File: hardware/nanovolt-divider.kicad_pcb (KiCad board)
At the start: 2 copper layers, 100 x 62 mm, 76 parts, among them J1 NORMAL IN +, J2 NORMAL IN -, J3 HV IN +, J4 HV IN -, J5 DIVIDER OUT HI, J6 DIVIDER OUT LO, J7 ESP32_DISP_P1, J8 ESP32_DISP_CN1, J9 ESP32_DISP_P3, K1 TQ2-L2-5V, K2 TQ2-L2-5V, K3 TQ2-L2-5V, K4 TQ2-L2-5V, K5 TQ2-L2-5V, Q1 MMBT2222A, Q10 MMBT2222A, Q2 MMBT2222A, Q3 MMBT2222A, Q4 MMBT2222A, Q5 MMBT2222A, Q6 MMBT2222A, Q7 MMBT2222A, Q8 MMBT2222A, Q9 MMBT2222A, SW1 SW_3PDT NORMAL/HV, U1 MCP23017-E/SO, U2 TMP117MAIYBGR

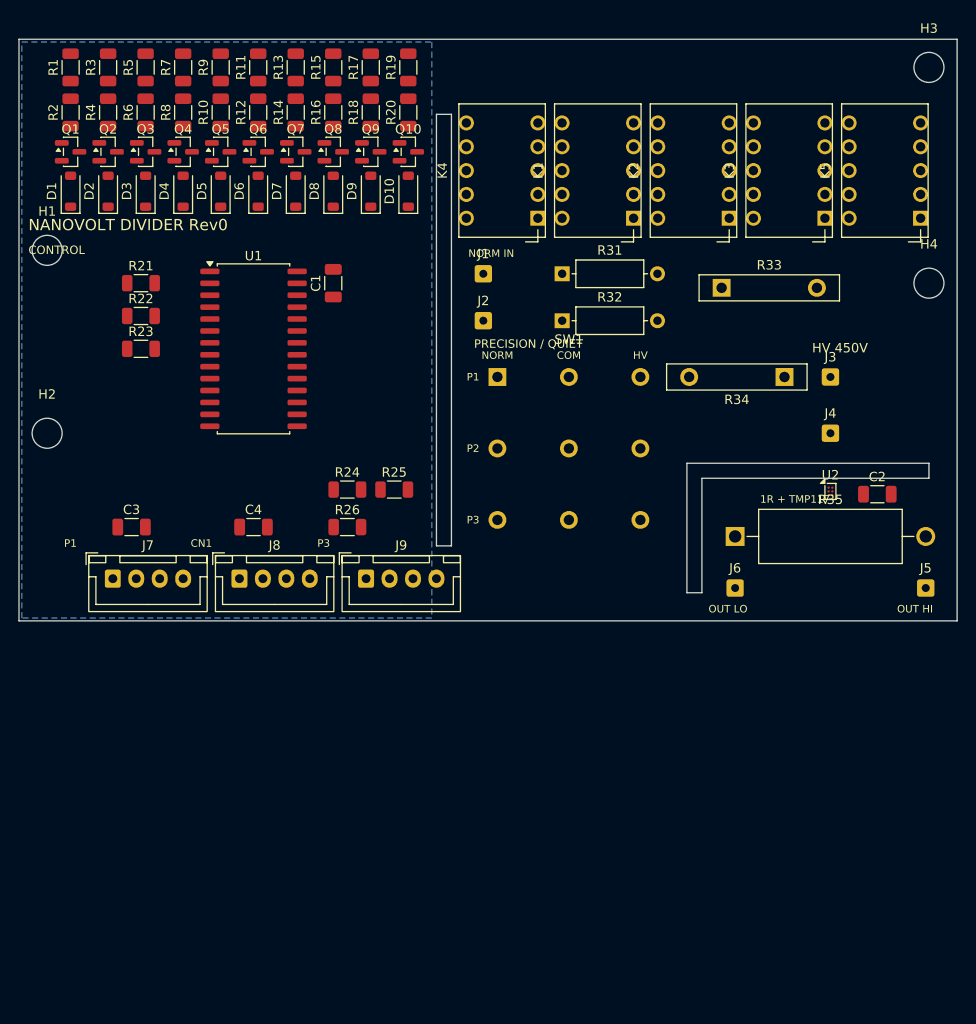
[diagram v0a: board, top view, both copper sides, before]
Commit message: PCB: portrait top-down layout, notch-isolated 1 ohm strip
- 60 x 103 mm: harness connectors, MCP23017 (horizontal, flanked by
  caps and pull-ups), coil drivers above their relays, relay row, then
  the quiet section (high legs, 3PDT pads, HV, 1 ohm strip)
- 1 ohm strip isolated by two edge notches with a 10 mm centre bridge
  for MEAS / return / TMP117 lines; driver-to-relay slot removed
- DRC: only unrouted ratsnest and silkscreen warnings remain

Co-Authored-By: Claude Fable 5.1 <noreply@anthropic.com>
Claude-Session: https://claude.ai/code/session_012iVAGTG9sDDBFakz9fB6fg
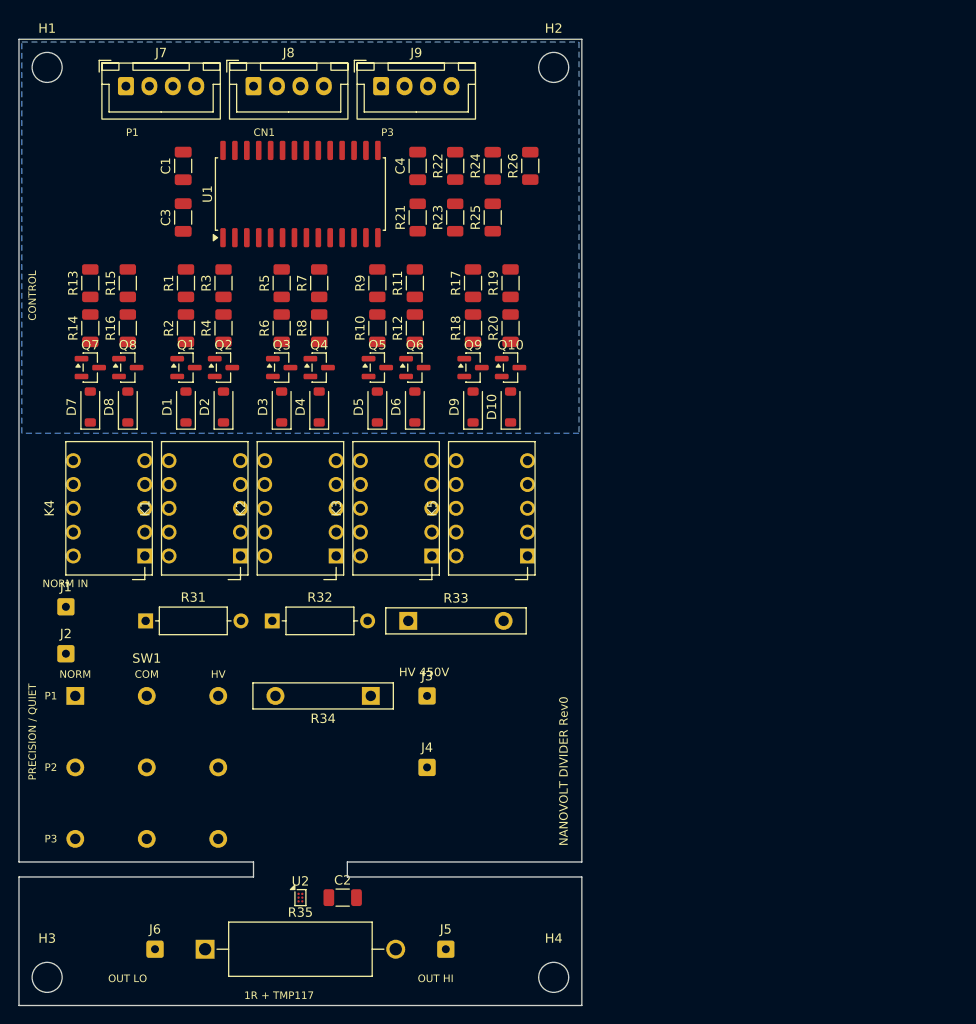
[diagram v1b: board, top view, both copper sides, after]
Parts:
- moved H3 135.1 mm to (53.0, 150.0)
- moved H4 84.1 mm to (107.0, 150.0)
- moved J6 72.8 mm to (64.5, 147.0)
- moved R35 71.6 mm to (69.8, 147.0)
- moved C2 71.4 mm to (84.5, 141.5)
- moved U2 71.2 mm to (80.0, 141.5)
- moved H2 66.6 mm to (107.0, 53.0)
- moved J5 64.0 mm to (95.5, 147.0)
- moved R31 57.8 mm to (63.5, 112.0)
- moved J1 56.9 mm to (55.0, 110.5)
- moved J2 56.9 mm to (55.0, 115.5)
- moved SW1 56.4 mm to (56.0, 120.0)
- moved J4 55.8 mm to (93.5, 127.6)
- moved R34 55.7 mm to (87.5, 120.0)
- moved K1 55.2 mm to (69.8, 100.0)
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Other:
- board size 100 x 62 mm -> 60 x 103 mm
